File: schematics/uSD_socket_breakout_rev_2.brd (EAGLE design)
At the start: 45.4 x 15.7 mm, 4 parts

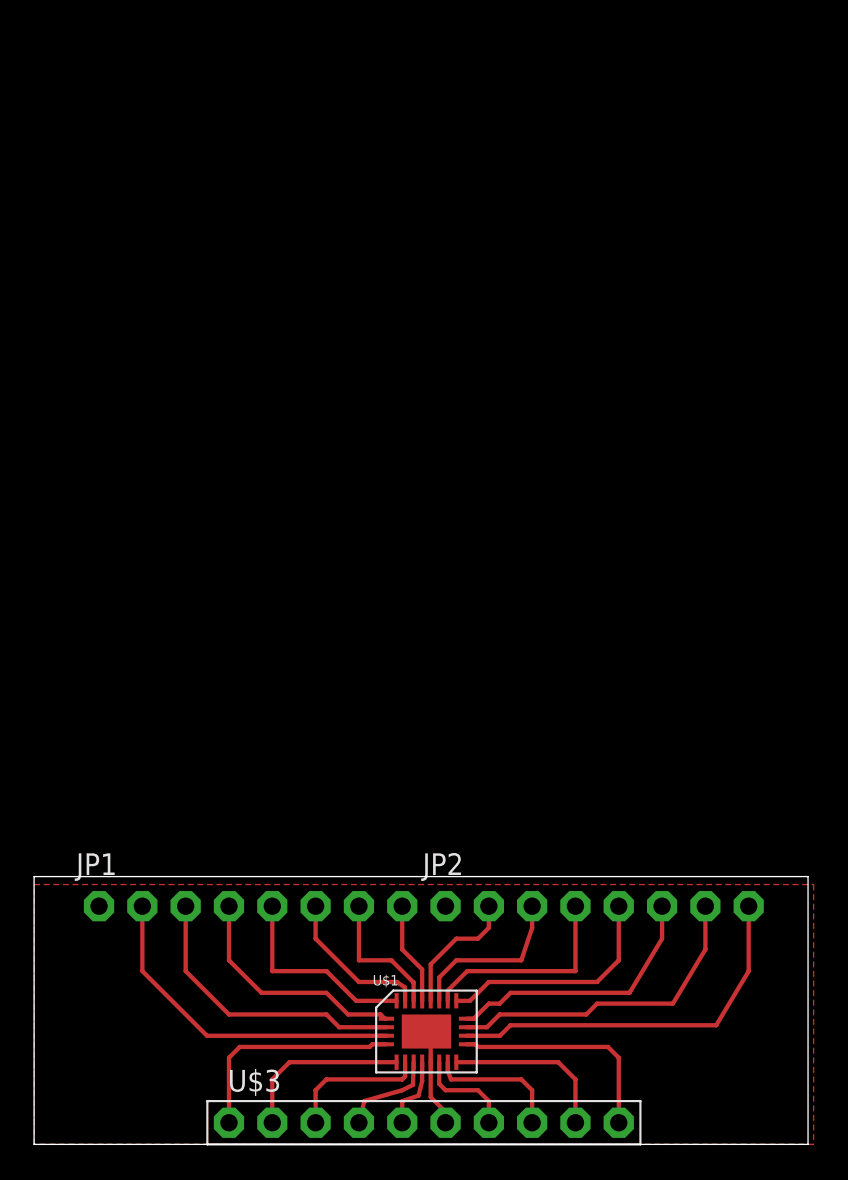
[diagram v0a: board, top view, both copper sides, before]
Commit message: Breakout boards for MUX and uSD socket, updated mux+uSD schematic
Built individual breakout boards for MUX chip and uSD socket.
Discovered errors in MUX and uSD integrated board and updated
schematic--ripped up wrong connections in .brd file but did not bother
rerouting traces since this board will most likely not be fabbed again.
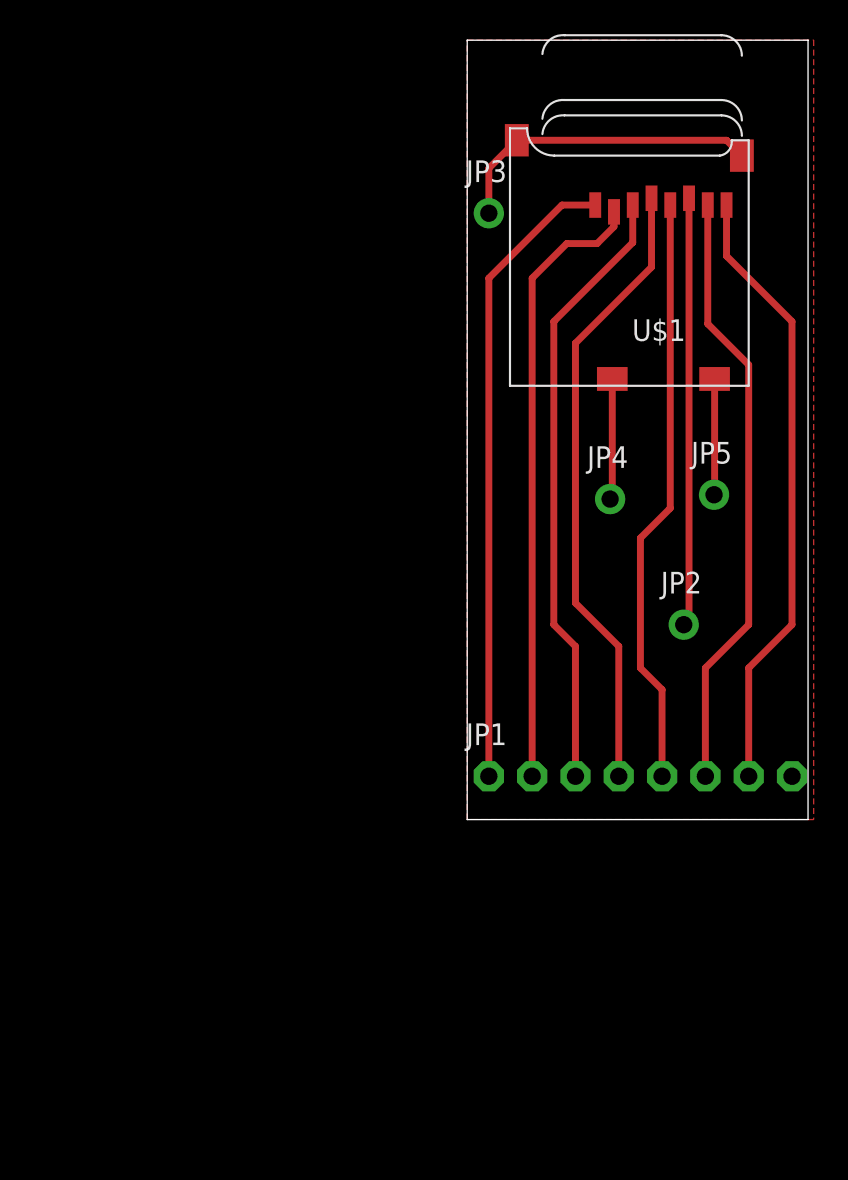
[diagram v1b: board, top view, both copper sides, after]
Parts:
- removed U$3: PINHD-1X10, adafruit:1X10-BIG
- added JP3, JP4, JP5: (no value), adafruit:1X01-CLEANBIG
- JP2: device adafruit:1X08-CLEANBIG -> adafruit:1X01-CLEANBIG
- U$1: value (none) -> MICROSD; device FSSD06_MLP24a:MLP-24 -> adafruit:MICROSD
- moved U$1 41.5 mm to (41.9, 44.5), turned to 180 degrees
- moved JP1 24.1 mm to (35.6, 21.6)
- moved JP2 17.3 mm to (38.1, 30.5)
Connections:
- removed net /OE: U$1./OE, U$3.1
- removed net 1CLK: JP1.6, U$1.1CLK
- removed net 1CMD: JP1.4, U$1.1CMD
- removed net 1DAT[0]: JP1.7, U$1.1DAT[0]
- removed net 1DAT[1]: JP1.8, U$1.1DAT[1]
- removed net 1DAT[2]: JP1.2, U$1.1DAT[2]
- removed net 1DAT[3]: JP1.3, U$1.1DAT[3]
- removed net 2CLK: JP2.6, U$1.2CLCK
- removed net 2CMD: JP2.4, U$1.2CMD
- removed net 2DAT3: JP2.3, U$1.2DAT[3]
- removed net 2DAT[0]: JP2.7, U$1.2DAT[0]
- removed net 2DAT[1]: JP2.8, U$1.2DAT[1]
- removed net 2DAT[2]: JP2.2, U$1.2DAT[2]
- removed net DAT[0]: U$1.DAT[0], U$3.8
- removed net S: U$1.S, U$3.10
- removed net VDDC1: JP1.5, U$1.VDDC1
- removed net VDDC2: JP2.5, U$1.VDDC2
- new net DAT0: JP1.6, U$1.7
- new net N$3: JP5.1, U$1.CD1
- new net N$4: JP4.1, U$1.CD2
- new net VSS: JP2.1, U$1.6
- net CLK: now also JP1.5, U$1.5; no longer U$1.CLK, U$3.7
- net CMD: now also JP1.3, U$1.3; no longer U$1.CMD, U$3.4
- net DAT[1]: now also JP1.7, U$1.8; no longer U$1.DAT[1], U$3.9
- net DAT[2]: now also JP1.1, U$1.1; no longer U$1.DAT[2], U$3.2
- net DAT[3]: now also JP1.2, U$1.2; no longer U$1.DAT[3], U$3.3
- net GND: now also JP3.1, U$1.MT1, U$1.MT2; no longer U$1.GND0, U$1.GND1, U$3.6
- net VDDH: now also JP1.4, U$1.4; no longer U$1.VDDH, U$3.5
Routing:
- net DAT0: track 0.00 -> 35.5 mm
- net VDDH: track 4.26 -> 36.8 mm
- net CMD: track 5.66 -> 35.9 mm
- net CLK: track 5.87 -> 34.8 mm
- net DAT[3]: track 8.33 -> 36.1 mm
- net DAT[2]: track 10.2 -> 37.2 mm
- net DAT[1]: track 9.95 -> 36.1 mm
- net VSS: track 0.00 -> 25.1 mm
- net 2DAT[1]: track 22.4 -> 0.00 mm
- net 1DAT[2]: track 19.7 -> 0.00 mm
- net 2DAT[0]: track 18.9 -> 0.00 mm
- net 1DAT[3]: track 16.9 -> 0.00 mm
- net 2CLK: track 15.8 -> 0.00 mm
- net 1CMD: track 13.8 -> 0.00 mm
- net VDDC2: track 13.7 -> 0.00 mm
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- added copper zone on layer 1, net GND
- removed copper zone on layer 1, net N$24
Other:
- board size 45.4 x 15.7 mm -> 20 x 45.7 mm
